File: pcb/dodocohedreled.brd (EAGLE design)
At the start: 50 x 47.5 mm, 11 parts

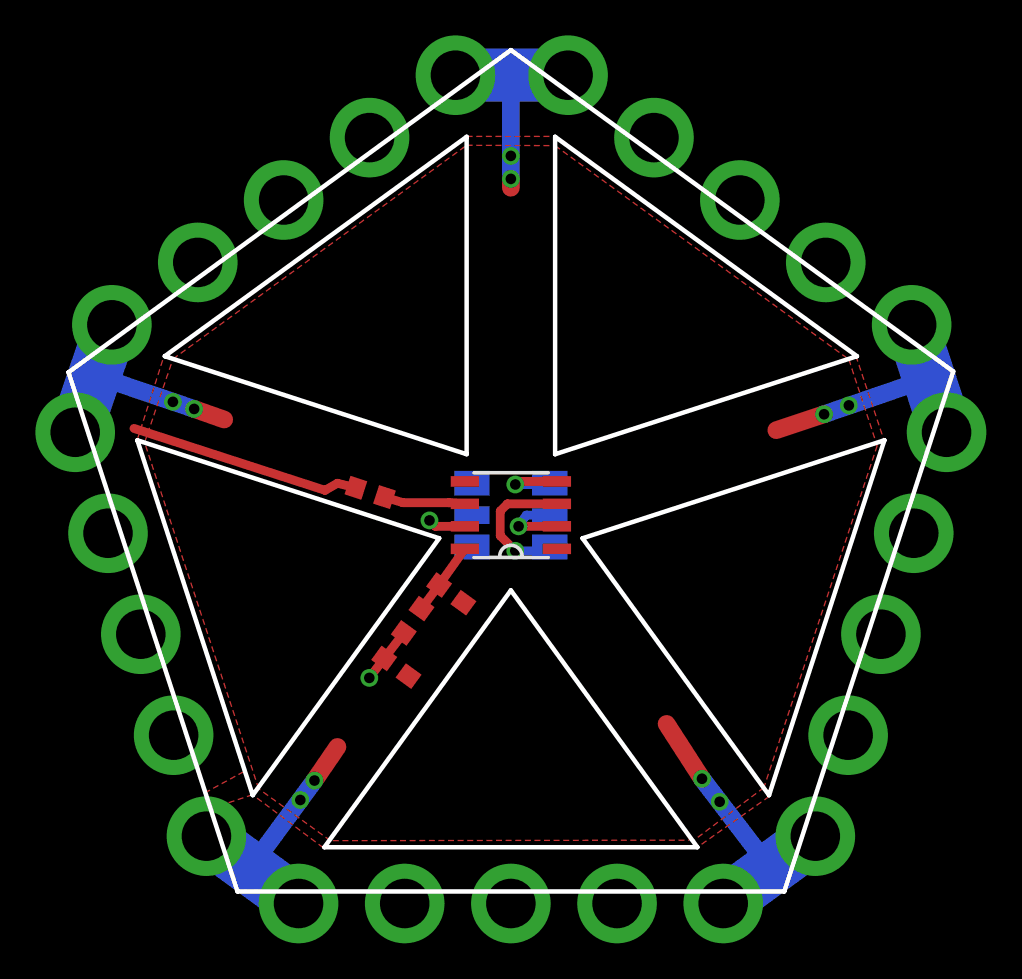
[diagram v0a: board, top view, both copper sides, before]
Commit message: Move all components to top side
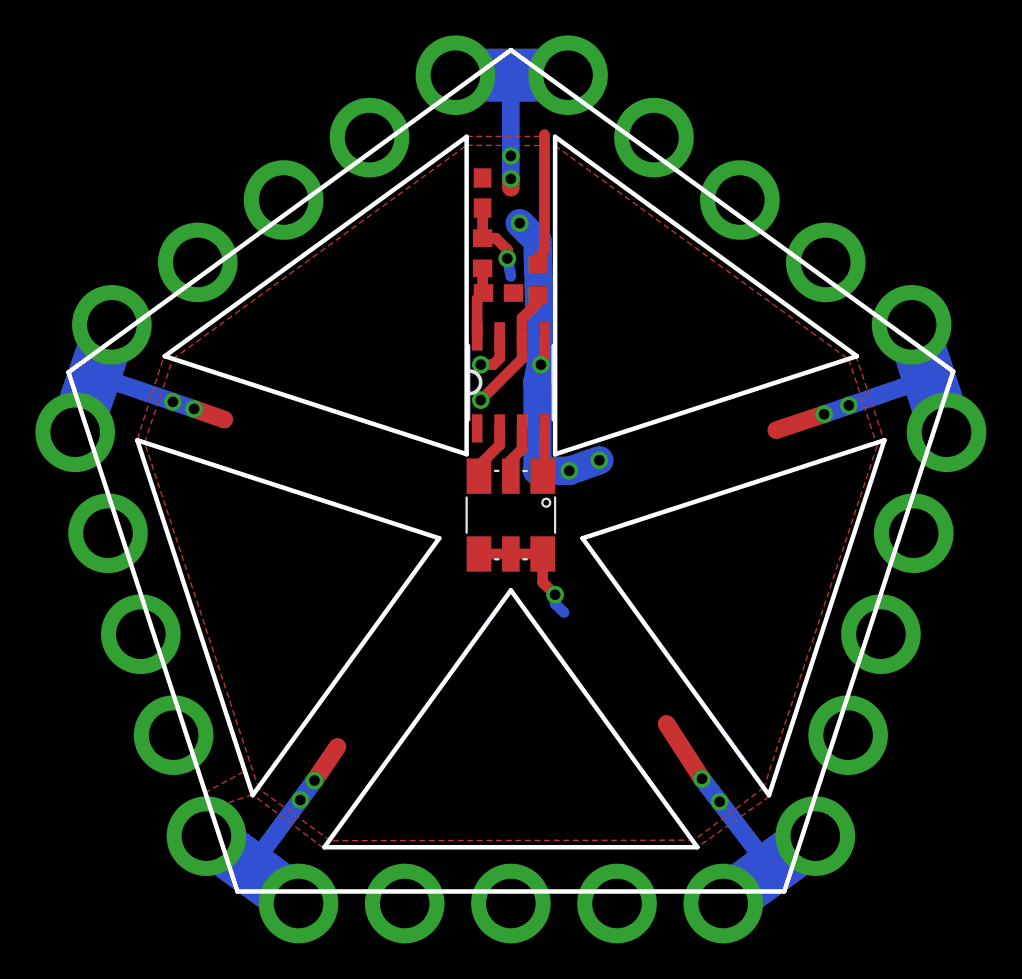
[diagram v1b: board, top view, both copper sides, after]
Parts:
- moved C2 27.2 mm to (-1.60, 18.2), turned to 90 degrees
- moved R1 21.1 mm to (-1.60, 14.8), turned to 90 degrees
- moved C1 17.2 mm to (-0.70, 12.6), turned to 0 degrees
- moved R2 15.3 mm to (1.55, 13.3), turned to 90 degrees
- moved U$1 7.50 mm to (0.00, 7.50), turned to 0 degrees
- flipped LED1 to the top, turned to 270 degrees
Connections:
- removed net N$4: LED1.2, U$1.2
- new net N$1: LED1.3, U$1.2
- net N$3: now also LED1.2; no longer LED1.3
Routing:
- net GND: track 90.0 -> 109.7 mm, vias 10 -> 14
- net 5V: track 3.20 -> 12.3 mm, vias 1 -> 2
- net DATA: track 13.2 -> 7.49 mm
- net N$3: track 8.01 -> 2.96 mm, vias 1 -> 0
- net N$4: track 4.26 -> 0.00 mm, vias 1 -> 0
- net N$1: track 0.00 -> 3.18 mm
- net N$10: track 4.59 -> 7.28 mm, vias 0 -> 1
- net N$2: track 4.40 -> 2.74 mm, vias 1 -> 0

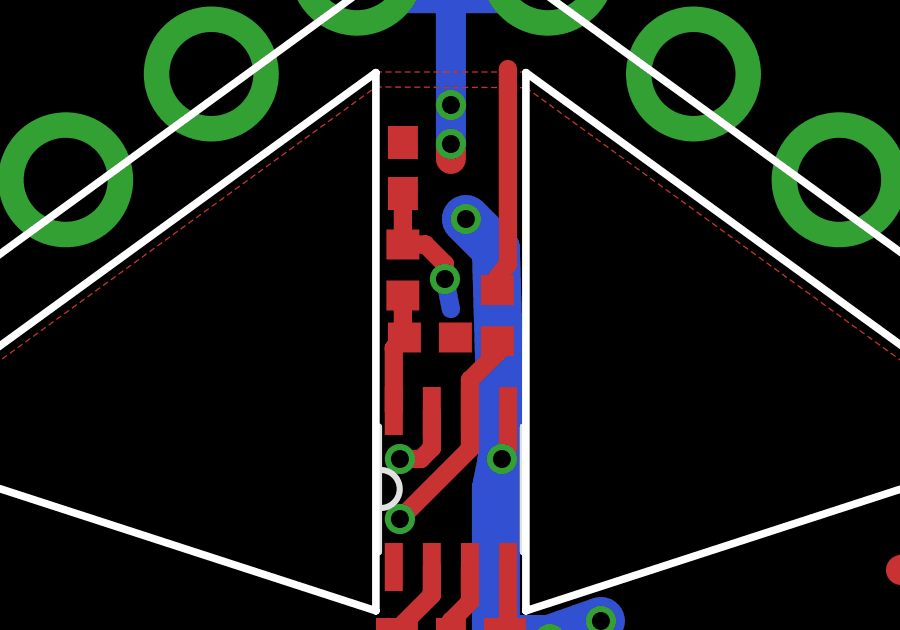
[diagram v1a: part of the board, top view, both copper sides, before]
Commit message: Add stop mask to test points.
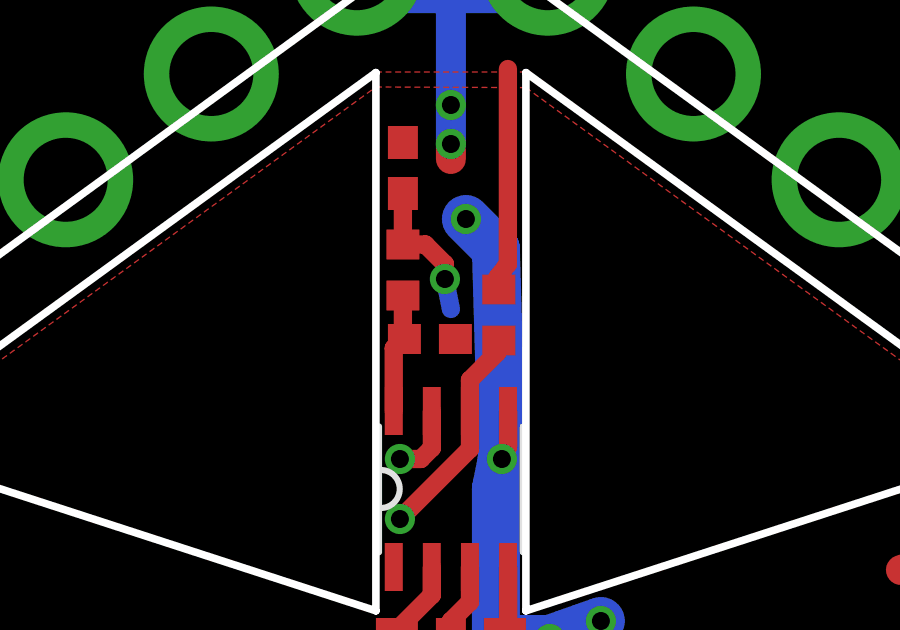
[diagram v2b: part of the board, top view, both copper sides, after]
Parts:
- moved R2 0.05 mm to (1.60, 13.3)
- moved C1 0.05 mm to (-0.70, 12.5)
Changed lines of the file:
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@@
 <element name="LED1" library="blinkinlabs" package="LED-TRICOLOR-5050-FIXED" value="LED-TRICOLOR-5050&quot;" x="0" y="0" smashed="yes" rot="R270"/>
 <element name="U$1" library="dodocohedreled" package="SOP8" value="WS2821A" x="0" y="7.5" smashed="yes"/>
-<element name="C1" library="adafruit" package="C0603" value=".1uF" x="-0.7" y="12.55" smashed="yes"/>
+<element name="C1" library="adafruit" package="C0603" value=".1uF" x="-0.7" y="12.5" smashed="yes"/>
 <element name="C2" library="adafruit" package="C0603" value="1uF" x="-1.6" y="18.2" smashed="yes" rot="R90"/>
 <element name="R1" library="adafruit" package="R0603" value="10" x="-1.6" y="14.8" smashed="yes" rot="R90"/>
-<element name="R2" library="adafruit" package="R0603" value="1k" x="1.55" y="13.28" smashed="yes" rot="R90"/>
+<element name="R2" library="adafruit" package="R0603" value="1k" x="1.6" y="13.3" smashed="yes" rot="R90"/>
 <element name="U$2" library="dodocohedreled" package="D_EDGE" value="D_EDGE" x="0" y="-21.2"/>
 <element name="U$3" library="dodocohedreled" package="D_EDGE" value="D_EDGE" x="20.2" y="-6.5" rot="R72"/>
@@
 <wire x1="-0.85" y1="15.65" x2="-0.2" y2="15" width="0.6096" layer="1"/>
 <wire x1="-0.2" y1="15" x2="-0.2" y2="14.5" width="0.6096" layer="1"/>
-<via x="-0.2" y="14.5" extent="1-16" drill="0.6"/>
+<via x="-0.2" y="14.5" extent="1-16" drill="0.6" alwaysstop="yes"/>
 <wire x1="-0.2" y1="14.5" x2="0" y2="13.5" width="0.6096" layer="16"/>
 <wire x1="-1.6" y1="17.35" x2="-1.6" y2="15.65" width="0.6096" layer="1"/>
@@
 <wire x1="1.905" y1="10.1" x2="1.905" y2="8.905" width="0.6096" layer="1"/>
 <wire x1="1.905" y1="8.905" x2="1.7" y2="8.5" width="0.6096" layer="1"/>
-<via x="1.7" y="8.5" extent="1-16" drill="0.6"/>
+<via x="1.7" y="8.5" extent="1-16" drill="0.6" alwaysstop="yes"/>
 </signal>
 <signal name="N$6">
@@
 <contactref element="R1" pad="1"/>
 <wire x1="-1.905" y1="10.1" x2="-1.905" y2="12.195" width="0.6096" layer="1"/>
-<wire x1="-1.905" y1="12.195" x2="-1.55" y2="12.55" width="0.6096" layer="1"/>
+<wire x1="-1.905" y1="12.195" x2="-1.55" y2="12.5" width="0.6096" layer="1"/>
 <wire x1="-1.6" y1="13.95" x2="-1.6" y2="12.6" width="0.6096" layer="1"/>
-<wire x1="-1.6" y1="12.6" x2="-1.55" y2="12.55" width="0.6096" layer="1"/>
+<wire x1="-1.6" y1="12.6" x2="-1.55" y2="12.5" width="0.6096" layer="1"/>
 </signal>
 <signal name="ADDR">
 <contactref element="U$1" pad="7"/>
-<via x="-1.7" y="8.5" extent="1-16" drill="0.6"/>
+<via x="-1.7" y="8.5" extent="1-16" drill="0.6" alwaysstop="yes"/>
 <wire x1="-1.7" y1="8.5" x2="-1" y2="8.5" width="0.6096" layer="1"/>
 <wire x1="-0.635" y1="10.1" x2="-0.635" y2="8.865" width="0.6096" layer="1"/>
@@
 <contactref element="U$1" pad="6"/>
 <contactref element="R2" pad="1"/>
-<wire x1="1.55" y1="12.43" x2="1.55" y2="12.05" width="0.6096" layer="1"/>
+<wire x1="1.6" y1="12.45" x2="1.55" y2="12.05" width="0.6096" layer="1"/>
 <wire x1="1.55" y1="12.05" x2="0.635" y2="11.135" width="0.6096" layer="1"/>
-<via x="-1.7" y="6.5" extent="1-16" drill="0.6"/>
+<via x="-1.7" y="6.5" extent="1-16" drill="0.6" alwaysstop="yes"/>
 <wire x1="0.635" y1="11.135" x2="0.635" y2="10.1" width="0.6096" layer="1"/>
 <wire x1="0.635" y1="10.1" x2="0.635" y2="8.835" width="0.6096" layer="1"/>
@@
 <vertex x="-17" y="-16.6"/>
 </polygon>
-<wire x1="1.55" y1="14.13" x2="1.55" y2="14.55" width="0.6096" layer="1"/>
+<wire x1="1.6" y1="14.15" x2="1.55" y2="14.55" width="0.6096" layer="1"/>
 <wire x1="1.55" y1="14.55" x2="1.9" y2="15" width="0.6096" layer="1"/>
 <wire x1="1.9" y1="15" x2="1.9" y2="21.5" width="0.6096" layer="1"/>
